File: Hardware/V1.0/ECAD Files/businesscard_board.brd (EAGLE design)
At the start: 54 x 85.6 mm, 31 parts, among them Y1 16MHz

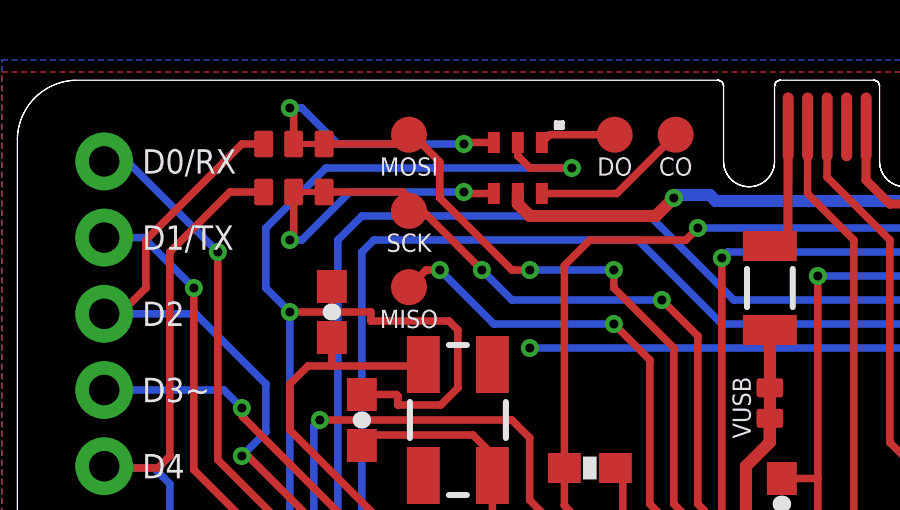
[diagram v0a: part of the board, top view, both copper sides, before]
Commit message: Fix APA102 pinout
Fix APA102 pinout, clean up library
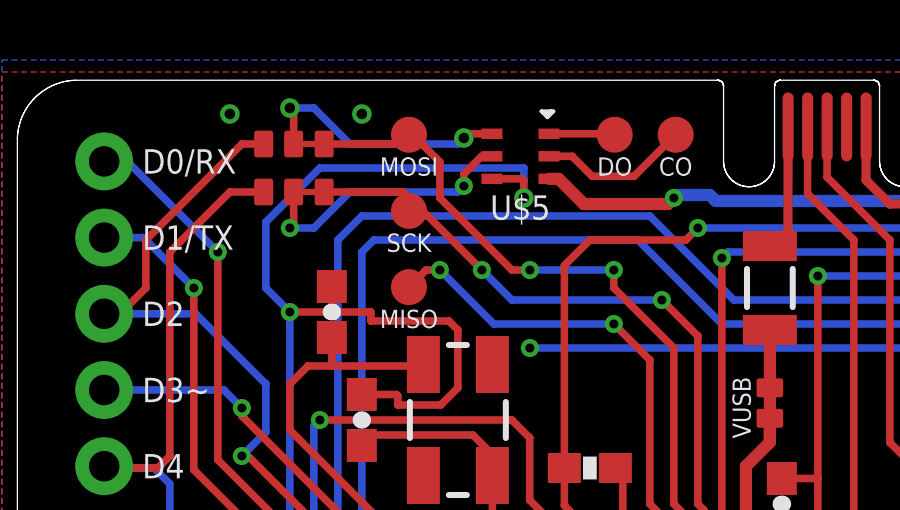
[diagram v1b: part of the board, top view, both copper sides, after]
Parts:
- removed D1: APA102-2020, PCBusinessCard:APA102-2020
- added U$5: (no value), businesscard_board:APA102_2020
- C1, C10, C2, C3, C4, C5, C6: device PCBusinessCard:0603-CAP -> businesscard_board:0603-CAP
- CO, DO, MISO, MOSI, SCK: device PCBusinessCard:TP12R -> businesscard_board:TP12R
- D2-/-°-MOSI, D4-/-°-SCK: device PCBusinessCard:SOLDER_JP_3WAY -> businesscard_board:SOLDER_JP_3WAY
- F1: device PCBusinessCard:PTC-1206 -> businesscard_board:PTC-1206
- L, ON, RX, TX: device PCBusinessCard:LED-0603_NOMARKER -> businesscard_board:LED-0603_NOMARKER
- R2, R5, R7: device PCBusinessCard:0603-RES -> businesscard_board:0603-RES
- RN2: device PCBusinessCard:CTS742C083 -> businesscard_board:CTS742C083
- RST_SW: device PCBusinessCard:EVPBB0AAB000 -> businesscard_board:EVPBB0AAB000
- U$1: value ATMEGA32U4 -> 32U4; device PCBusinessCard:TQFP44_QRCODE -> businesscard_board:TQFP44_QRCODE
- U$2: device PCBusinessCard:ARDUINO_BC_SINGLEROWS -> businesscard_board:ARDUINO_BC_SINGLEROWS
- U$3: device PCBusinessCard:TOUCH_SENSORS -> businesscard_board:TOUCH_SENSORS
- U$4: device PCBusinessCard:USB_TYPE_B_SS_2_NO_DIMENSION -> businesscard_board:USB_TYPE_B_SS_2_NO_DIMENSION
- VUSB: device PCBusinessCard:SOLDER_JP -> businesscard_board:SOLDER_JP
- Y1: device PCBusinessCard:CRYSTAL-SMD-5X3 -> businesscard_board:CRYSTAL-SMD-5X3
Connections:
- removed net N$7: D1.SDO, DO.TP
- removed net N$8: D1.SDI, D2-/-°-MOSI.2
- removed net N$9: D1.CKI, D4-/-°-SCK.2
- new net APA102_CI: D4-/-°-SCK.2, U$5.5
- new net APA102_CO: CO.TP, U$5.2
- new net APA102_DO: DO.TP, U$5.1
- net GND: now also U$5.4; no longer D1.GND
- net N$6: now also D2-/-°-MOSI.2, U$5.6; no longer CO.TP, D1.CKO
- net VCC: now also U$5.3; no longer D1.VDD
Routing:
- net APA102_CI: track 0.00 -> 9.21 mm, vias 0 -> 2
- net N$9: track 9.14 -> 0.00 mm, vias 2 -> 0
- net N$8: track 8.57 -> 0.00 mm, vias 2 -> 0
- net APA102_CO: track 0.00 -> 5.07 mm
- net N$6: track 5.27 -> 8.63 mm, vias 0 -> 2
- net N$7: track 2.54 -> 0.00 mm
- net APA102_DO: track 0.00 -> 2.20 mm
- net VCC: track 166.0 -> 164.6 mm
- net GND: track 319.9 -> 318.6 mm, vias 15 -> 17
